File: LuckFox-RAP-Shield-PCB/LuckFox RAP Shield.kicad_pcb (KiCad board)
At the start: 2 copper layers, 45 x 63.2 mm, 9 parts, among them J1 LuckFox_Pico_Mini_Connector, J2 External_5V_Input_from_Buck_M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, U2 W5500_Ethernet_Module_DNP_on_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

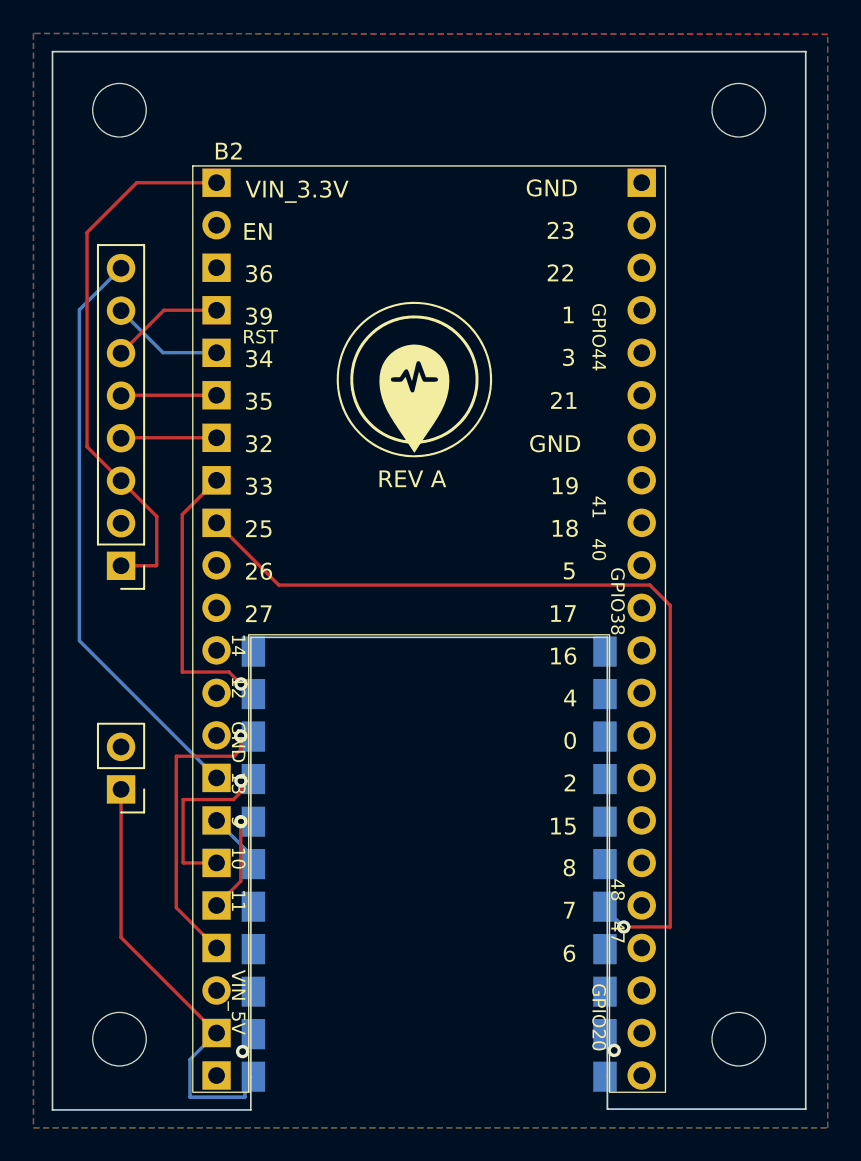
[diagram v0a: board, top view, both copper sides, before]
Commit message: Push PCB copper/mask/edge clearance to manufacturer spec where physically possible
Compared the board against a manufacturer's stated minimums (track/space,
via size, solder mask expansion, edge clearance, silkscreen line width)
and pushed each toward spec via DRC bisection rather than guessing:

- Solder mask expansion: 0 -> 0.095mm (spec 0.1016mm; verified safe max)
- Board edge clearance: 0 -> 0.254mm, extending the existing J1
  castellated-pad DRU exception to the GND/+5V_RAIL/GPIO15/16 nets that
  approach the same by-design edge zone (previously unflagged only
  because the global minimum was 0, not because they were actually clear)
- Track width / clearance / via size: confirmed via bisection to already
  sit at this layout's true physical ceiling (0.2mm / 0.2mm / 0.8mm) --
  the B2 header has zero spare copper margin, and pushing further
  reintroduces real short-circuit risk (shorting_items/solder_mask_bridge
  DRC errors), so left at their original values rather than forced
- Silkscreen minimum line width: attempted, reverted -- meeting it
  required growing pin-label text past the point where it stays clear of
  the module outline and board edge on this densely-labeled breakout
  footprint, trading a spec item that wasn't actually required (only
  line width was, not silk-to-silk/edge spacing) for new DRC warnings
  that didn't exist before

0 DRC errors. Also confirmed clearance/shorting/track-width checks are
already default "error" severity, not something needing manual opt-in.

Co-Authored-By: Claude Sonnet 5 <noreply@anthropic.com>
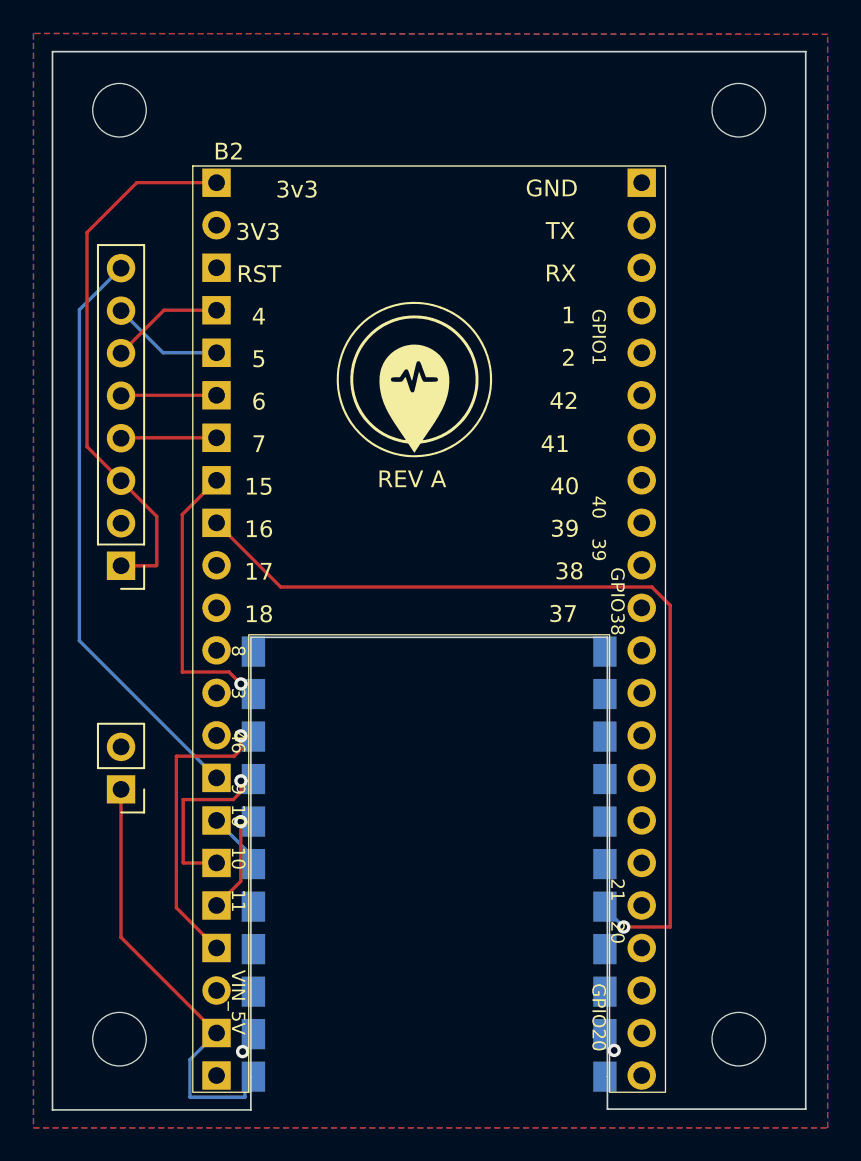
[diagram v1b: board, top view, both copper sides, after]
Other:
- rule pad_to_mask_clearance: 0 -> 0.095

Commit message: Fix W5500 SPI net mixup, bring copper fully to manufacturer spec, polish silkscreen
- Schematic: W5500's CS/SCK/MOSI/MISO were wired to the same ESP32 GPIO
  group LuckFox uses (Net-(B2-GPIO10-13_..._LF)) instead of its own
  dedicated group (GPIO4/5/6/7/9_..._ETH) -- real short/bus-conflict risk,
  not a false positive. Rewired to the correct pins.
- Reference designators B2/J1 had been accidentally renamed (to
  "ESP32-S3-Devkitc-1"/"Luckfox Pico Mini"), silently breaking the DRU
  exception that protects J1's spare castellated pads from false edge-
  clearance errors. Restored to "B2"/"J1".
- Copper brought to full manufacturer spec via real re-routing (not just
  loosened settings) -- track width 0.2->0.254mm, clearance 0.2->0.254mm,
  via 0.8/0.4->1.37-1.47mm/1mm (vias now sized/centered so their own
  drilled hole forms a proper semicircular castellation edge alongside
  LuckFox's own, once routed), solder mask expansion 0->0.1016mm, board
  edge clearance 0->0.254mm (extended the existing J1 DRU exception to
  the GND/+5V_RAIL/GPIO15/16 nets that share the same edge zone), zone
  min_thickness 0.25->0.254mm. All verified via DRC bisection against
  real geometry, including a proper --refill-zones pass each time (a
  plain width edit doesn't recompute the pour shape, which produced
  false zone-clearance violations during testing).
- Silkscreen line width and text thickness both brought to the 0.203mm
  spec. Text needed a wider stroke *and* larger character size together,
  since KiCad clamps effective stroke thickness to 25% of character
  height -- thickness alone was silently capped by the original 0.8mm
  size.
- Enlarged the board logo 1.2x (silhouette only, kept the original
  0.203mm line weight instead of scaling it 1:1, which read as too
  heavy), and made the 4 mounting holes symmetric on both axes with
  clean rounded coordinates (117/154 x, 78.9/134.3 y).

0 DRC errors, every numeric item on the target manufacturer's spec sheet
now met with real m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
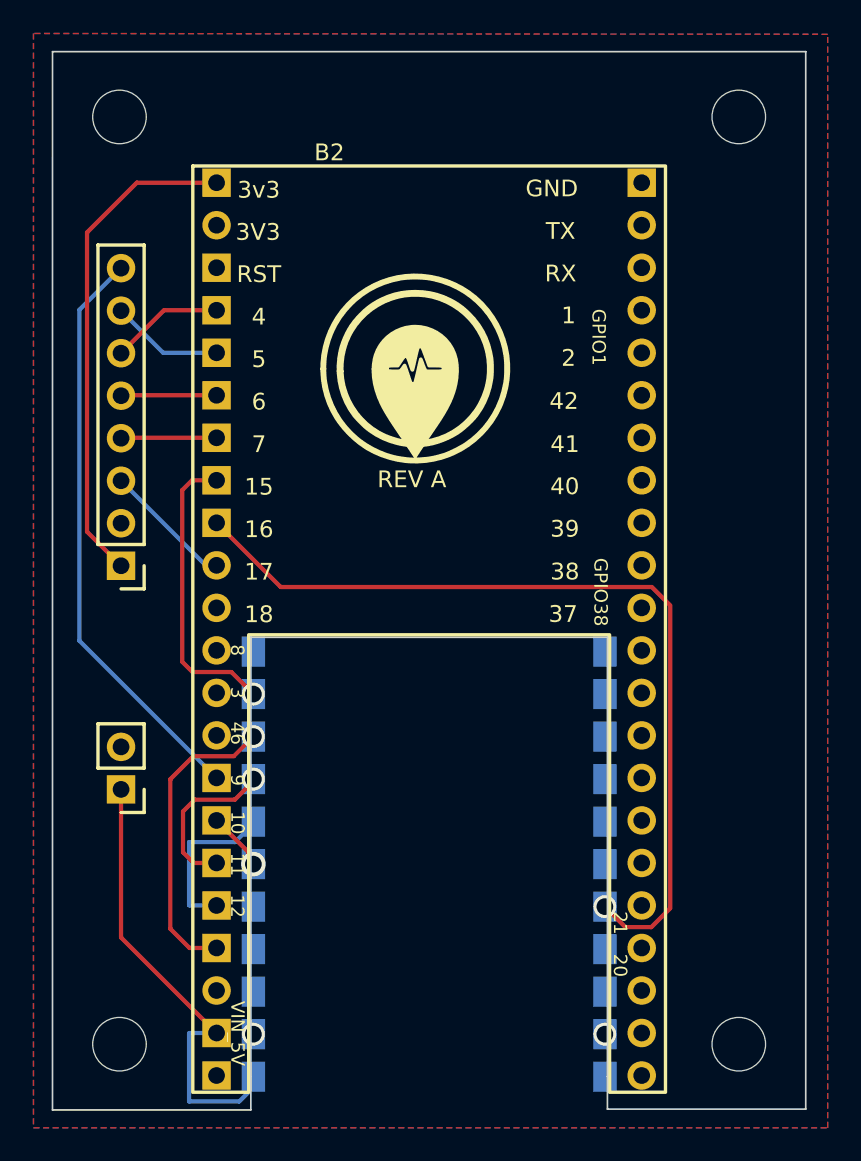
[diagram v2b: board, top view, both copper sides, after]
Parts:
- moved G*** 0.66 mm to (134.7, 93.9)
- moved H1 0.40 mm to (117.0, 78.9)
- moved H2 0.40 mm to (154.0, 78.9)
- moved H3 0.30 mm to (117.0, 134.3)
- moved H4 0.30 mm to (154.0, 134.3)
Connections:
- B2 pad 17: (no net) -> unconnected-(B2-3V3-Pad17)
- B2 pad 18: (no net) -> Net-(B2-GPIO17)
- B2 pad 19: (no net) -> unconnected-(B2-GPIO18-Pad19)
- B2 pad 20: (no net) -> unconnected-(B2-GPIO8-Pad20)
- B2 pad 21: (no net) -> unconnected-(B2-GPIO3-Pad21)
- B2 pad 22: (no net) -> unconnected-(B2-GPIO46-Pad22)
- B2 pad 23: (no net) -> unconnected-(B2-GPIO14-Pad23)
- B2 pad 24: (no net) -> unconnected-(B2-GPIO43-Pad24)
- B2 pad 25: (no net) -> unconnected-(B2-GPIO44-Pad25)
- B2 pad 26: (no net) -> unconnected-(B2-GPIO1-Pad26)
- B2 pad 27: (no net) -> unconnected-(B2-GPIO2-Pad27)
- B2 pad 28: (no net) -> unconnected-(B2-GPIO42-Pad28)
- B2 pad 29: (no net) -> unconnected-(B2-GPIO41-Pad29)
- B2 pad 30: (no net) -> unconnected-(B2-GPIO40-Pad30)
- B2 pad 31: (no net) -> unconnected-(B2-GPIO39-Pad31)
- B2 pad 32: (no net) -> unconnected-(B2-GPIO38-Pad32)
- B2 pad 33: (no net) -> unconnected-(B2-GPIO37-Pad33)
- B2 pad 34: (no net) -> unconnected-(B2-GPIO36-Pad34)
- B2 pad 35: (no net) -> unconnected-(B2-GPIO35-Pad35)
- B2 pad 36: (no net) -> unconnected-(B2-GPIO0-Pad36)
- B2 pad 37: (no net) -> unconnected-(B2-GPIO45-Pad37)
- B2 pad 38: (no net) -> unconnected-(B2-GPIO48-Pad38)
- B2 pad 39: (no net) -> unconnected-(B2-GPIO47-Pad39)
- B2 pad 40: (no net) -> unconnected-(B2-GPIO21-Pad40)
- B2 pad 41: (no net) -> unconnected-(B2-GPIO20-Pad41)
- B2 pad 42: (no net) -> unconnected-(B2-GPIO19-Pad42)
- B2 pad 43: (no net) -> GND
- B2 pad 44: (no net) -> GND
- U2 pad 3: +3V3_RAIL -> Net-(B2-GPIO17)
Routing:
- net Net-(B2-GPIO17): track 0.00 -> 7.80 mm
- net Net-(B2-GPIO12_SCK_LF): track 6.11 -> 9.36 mm, vias 1 -> 0
- net +3V3_RAIL: track 32.7 -> 29.7 mm
- net GND: track 1.20 -> 0.00 mm
- net Net-(B2-GPIO11_MOSI_LF): track 10.7 -> 9.67 mm
- net Net-(B2-GPIO16_SLAVE_RDY_OUT): track 52.7 -> 52.0 mm
- net Net-(B2-GPIO15_DATA_RDY_IN): track 17.0 -> 17.5 mm
- net Net-(B2-GPIO10_CS_LF): track 3.42 -> 3.41 mm, vias 0 -> 1
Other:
- rule pad_to_mask_clearance: 0.095 -> 0.1016

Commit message: Give J1 (LuckFox) pads real two-layer copper, drop the separate stitching vias
J1's castellated pads were SMD (B.Cu only), relying on 7 separate nearby
vias to bridge signals up to F.Cu for routing to the ESP32 header. Changed
each pad to a real through-hole feature (1.8x1.4mm flat pad, 1mm drill) so
the pad itself provides copper on both layers -- same technique as a
proper castellated edge (a full plated hole exactly on the board-edge cut
line, which becomes a plated half-moon once routed), just applied to the
component pads instead of a separate stitching via next to them. Removed
the now-redundant vias.

Most signal traces got moved to F.Cu to match their pads directly. SCK_LF
couldn't follow -- forcing it onto the same layer as MOSI_LF/CS_LF made
its path physically cross both of them, a real short risk given J1 and
B2's pin ordering don't allow a crossing-free single-layer path between
those three signals. Left SCK_LF's own pad on B.Cu instead of forcing a
new via, since its existing routing already terminates there safely.

Also fixed two real connectivity gaps this surfaced: both GND pads
weren't reaching the pour through the edge-castellation zone-fill (added
short explicit stitch traces), and resolved the silkscreen-over-copper
warnings from B2's labels now sitting next to real F.Cu copper at J1.

0 DRC errors and warnings.

Co-Authored-By: Claude Sonnet 5 <noreply@anthropic.com>
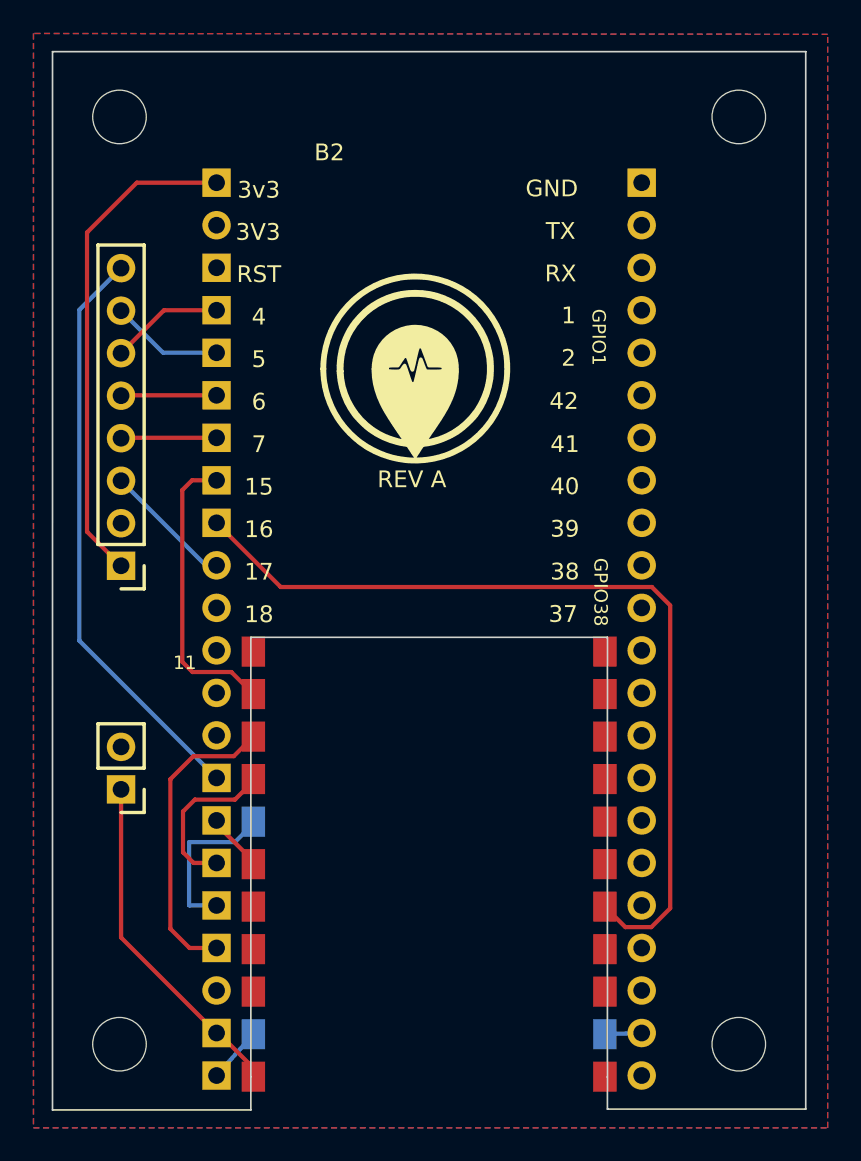
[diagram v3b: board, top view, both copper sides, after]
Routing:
- net +5V_RAIL: track 27.4 -> 20.4 mm
- net GND: track 0.00 -> 5.51 mm, vias 2 -> 0
- net Net-(B2-GPIO13_MISO_LF): vias 1 -> 0
- net Net-(B2-GPIO16_SLAVE_RDY_OUT): vias 1 -> 0
- net Net-(B2-GPIO15_DATA_RDY_IN): vias 1 -> 0
- net Net-(B2-GPIO11_MOSI_LF): vias 1 -> 0
- net Net-(B2-GPIO10_CS_LF): vias 1 -> 0

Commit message: Bring trace width and clearance to full 0.3mm manufacturer spec
Track width and clearance both needed to reach 0.3mm per this
manufacturer's requirements. Track width alone was fine, but clearance
was blocked near B2's through-hole header pins -- shrunk B2's pad
diameter 1.7mm -> 1.27mm (still at/above the manufacturer's own stated
via-diameter floor for double-layer boards, drill left at 1mm so real
header pins still fit) to free up the room. Verified via DRC: 0 errors
at 0.3mm track width and 0.3mm clearance simultaneously.

Also regenerated gerbers/STEP/drill files from the current board (the
committed ones were stale relative to this and the previous pad-layer
commit), using --board-plot-params to match the project's existing
KiCad-extension naming convention, and split drill output into PTH/NPTH
per the manufacturer's request for a drill file.

Co-Authored-By: Claude Sonnet 5 <noreply@anthropic.com>
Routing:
- net GND: track 5.51 -> 9.54 mm
